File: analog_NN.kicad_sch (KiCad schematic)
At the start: 0 parts

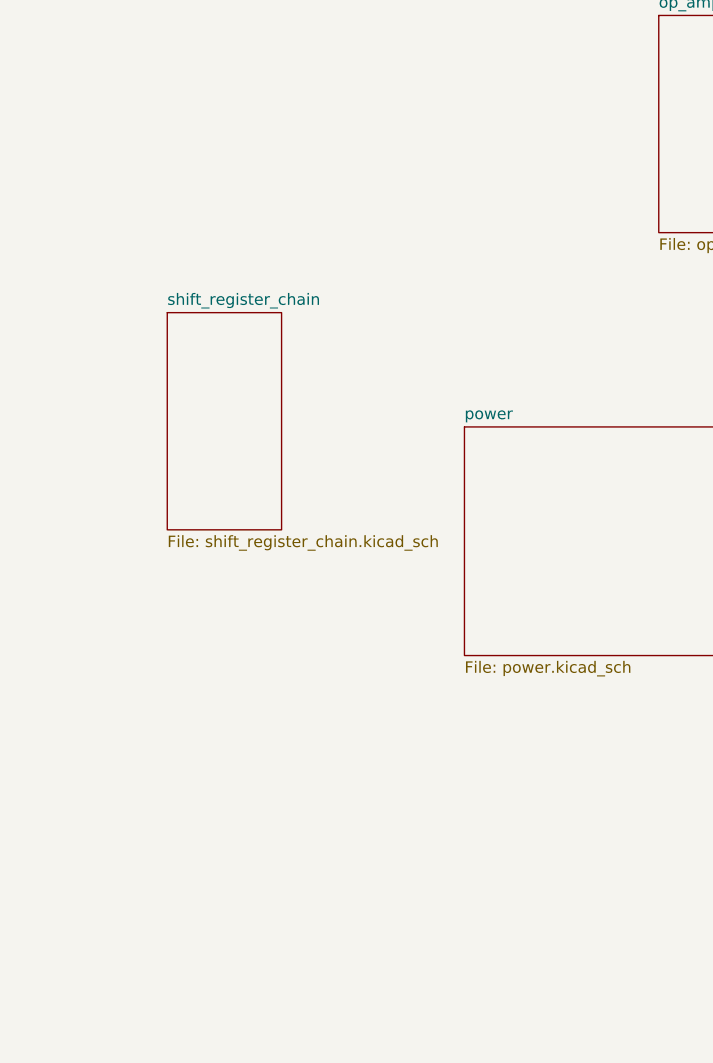
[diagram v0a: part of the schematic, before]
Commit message: Updated: crossbar
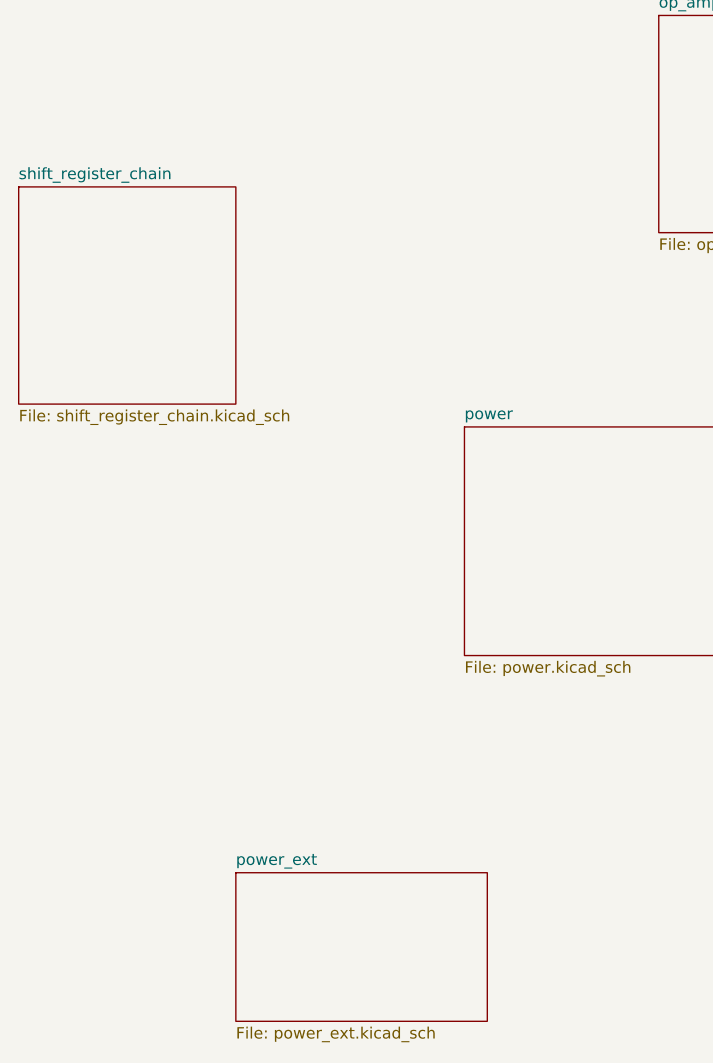
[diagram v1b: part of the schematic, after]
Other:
- added sheet power_ext (power_ext.kicad_sch)
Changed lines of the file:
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@@
 	)
 	(sheet
-		(at 48.26 114.3)
-		(size 12.7 24.13)
+		(at 31.75 100.33)
+		(size 24.13 24.13)
 		(exclude_from_sim no)
 		(in_bom yes)
@@
 		)
 		(property "Sheetname" "shift_register_chain"
-			(at 48.26 113.5884 0)
+			(at 31.75 99.6184 0)
 			(effects
 				(font
@@
 		)
 		(property "Sheetfile" "shift_register_chain.kicad_sch"
-			(at 48.26 139.0146 0)
+			(at 31.75 125.0446 0)
 			(effects
 				(font
@@
 				(path "/8de080c9-ac72-4350-b5d3-2d90d26f0ccc"
 					(page "9")
+				)
+			)
+		)
+	)
+	(sheet
+		(at 55.88 176.53)
+		(size 27.94 16.51)
+		(exclude_from_sim no)
+		(in_bom yes)
+		(on_board yes)
+		(dnp no)
+		(fields_autoplaced yes)
+		(stroke
+			(width 0.1524)
+			(type solid)
+		)
+		(fill
+			(color 0 0 0 0.0000)
+		)
+		(property "Sheetname" "power_ext"
+			(at 55.88 175.8184 0)
+			(effects
+				(font
+					(size 1.27 1.27)
+				)
+				(justify left bottom)
+			)
+		)
+		(property "Sheetfile" "power_ext.kicad_sch"
+			(at 55.88 193.6246 0)
+			(effects
+				(font
+					(size 1.27 1.27)
+				)
+				(justify left top)
+			)
+		)
+		(instances
+			(project "analog_NN"
+				(path "/8de080c9-ac72-4350-b5d3-2d90d26f0ccc"
+					(page "10")
 				)
 			)
@@
 		(exclude_from_sim no)
 		(in_bom yes)
-		(on_board yes)
+		(on_board no)
 		(dnp no)
 		(fields_autoplaced yes)

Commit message: Updated: export material
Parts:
- added H1, H2, H3, H4: MountingHole, MountingHole:MountingHole_3.2mm_M3, symbol Mechanical:MountingHole
